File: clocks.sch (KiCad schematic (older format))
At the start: 13 parts, among them J9 UPDI TTL, U10 ATtiny1614-SS, U11 5M1270ZT144C5N, U14 Si5351A-B-GT, X1 CB3LV-3I-100M0000, Y1 25MHZ 8PF

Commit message: parts placement
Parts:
- U10: Description (none) -> 8-bit Microcontrollers - MCU 20MHZ SOIC 85C GRN; MFR (none) -> Microchip Technology; MPN (none) -> ATTINY1614-SSNR; SPN (none) -> 556-ATTINY1614SSNR; SPR (none) -> Mouser; SPURL (none) -> https://www.mouser.com/ProductDetail/556-ATTINY1614SSNR
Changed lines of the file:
@@
 F 2 "Package_SO:SOIC-14_3.9x8.7mm_P1.27mm" H 2150 4660 50  0001 C CIN
 F 3 "http://ww1.microchip.com/downloads/en/DeviceDoc/ATtiny1614-data-sheet-40001995A.pdf" H 2150 4660 50  0001 C CNN
+F 4 "8-bit Microcontrollers - MCU 20MHZ SOIC 85C GRN" H 2150 4660 50  0001 C CNN "Description"
+F 5 "Microchip Technology" H 2150 4660 50  0001 C CNN "MFR"
+F 6 "ATTINY1614-SSNR" H 2150 4660 50  0001 C CNN "MPN"
+F 7 "556-ATTINY1614SSNR" H 2150 4660 50  0001 C CNN "SPN"
+F 8 "Mouser" H 2150 4660 50  0001 C CNN "SPR"
+F 9 "https://www.mouser.com/ProductDetail/556-ATTINY1614SSNR" H 2150 4660 50  0001 C CNN "SPURL"
 	1    2150 4660
 	1    0    0    -1

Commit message: started routing
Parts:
- removed C33: 100nF, Capacitor_SMD:C_0603_1608Metric_Pad1.05x0.95mm_HandSolder, symbol Device:C
- removed R12: 22R5, Resistor_SMD:R_0603_1608Metric_Pad1.05x0.95mm_HandSolder, symbol Device:R_Small
- removed X1: CB3LV-3I-100M0000, Oscillator:Oscillator_SMD_SeikoEpson_SG8002CA-4Pin_7.0x5.0mm_HandSoldering, symbol rc2014_max_v-rescue:CB3LV-3I-50M0000-Oscillator
- J9: footprint Connector_PinHeader_2.54mm:PinHeader_1x03_P2.54mm_Horizontal -> Connector_PinHeader_2.54mm:PinHeader_1x03_P2.54mm_Vertical
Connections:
- net labels added: CLK2_F
- net labels removed: CLK_50Mhz
- wire segments 43 -> 30
- no-connect marks 9 -> 10
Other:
- moved on the sheet: R10, R11, U14, Y1

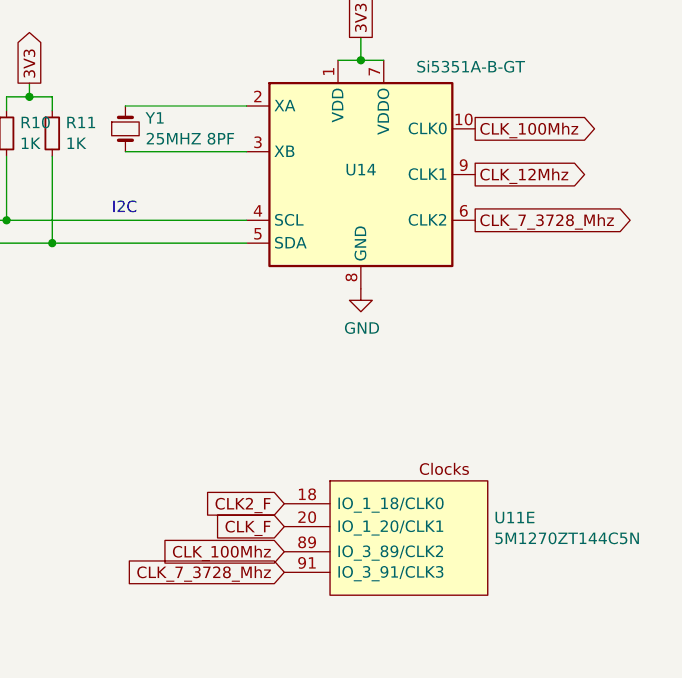
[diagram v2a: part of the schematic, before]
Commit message: moved things around to improve routing, fixed power plane
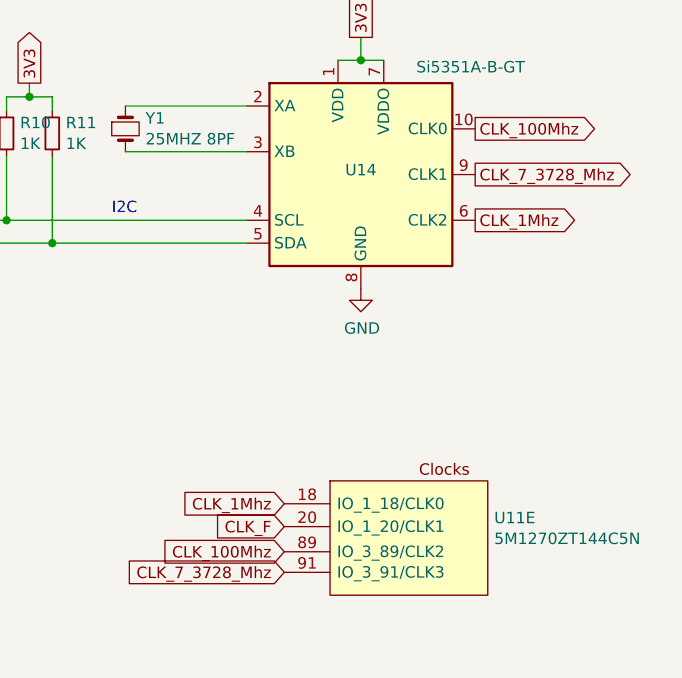
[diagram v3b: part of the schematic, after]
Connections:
- net labels added: CLK_1Mhz
- net labels removed: CLK2_F, CLK_12Mhz
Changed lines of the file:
@@
 CLK_100Mhz
 Text GLabel 6335 1845 2    50   Output ~ 0
-CLK_12Mhz
-Text GLabel 6335 2045 2    50   Output ~ 0
 CLK_7_3728_Mhz
 Text GLabel 4175 2045 0    50   BiDi ~ 0
@@
 NoConn ~ 1550 4460
 NoConn ~ 3415 4055
+Text GLabel 6335 2045 2    50   Output ~ 0
+CLK_1Mhz
 Text GLabel 5500 3285 0    50   Input ~ 0
-CLK2_F
+CLK_1Mhz
 $EndSCHEMATC

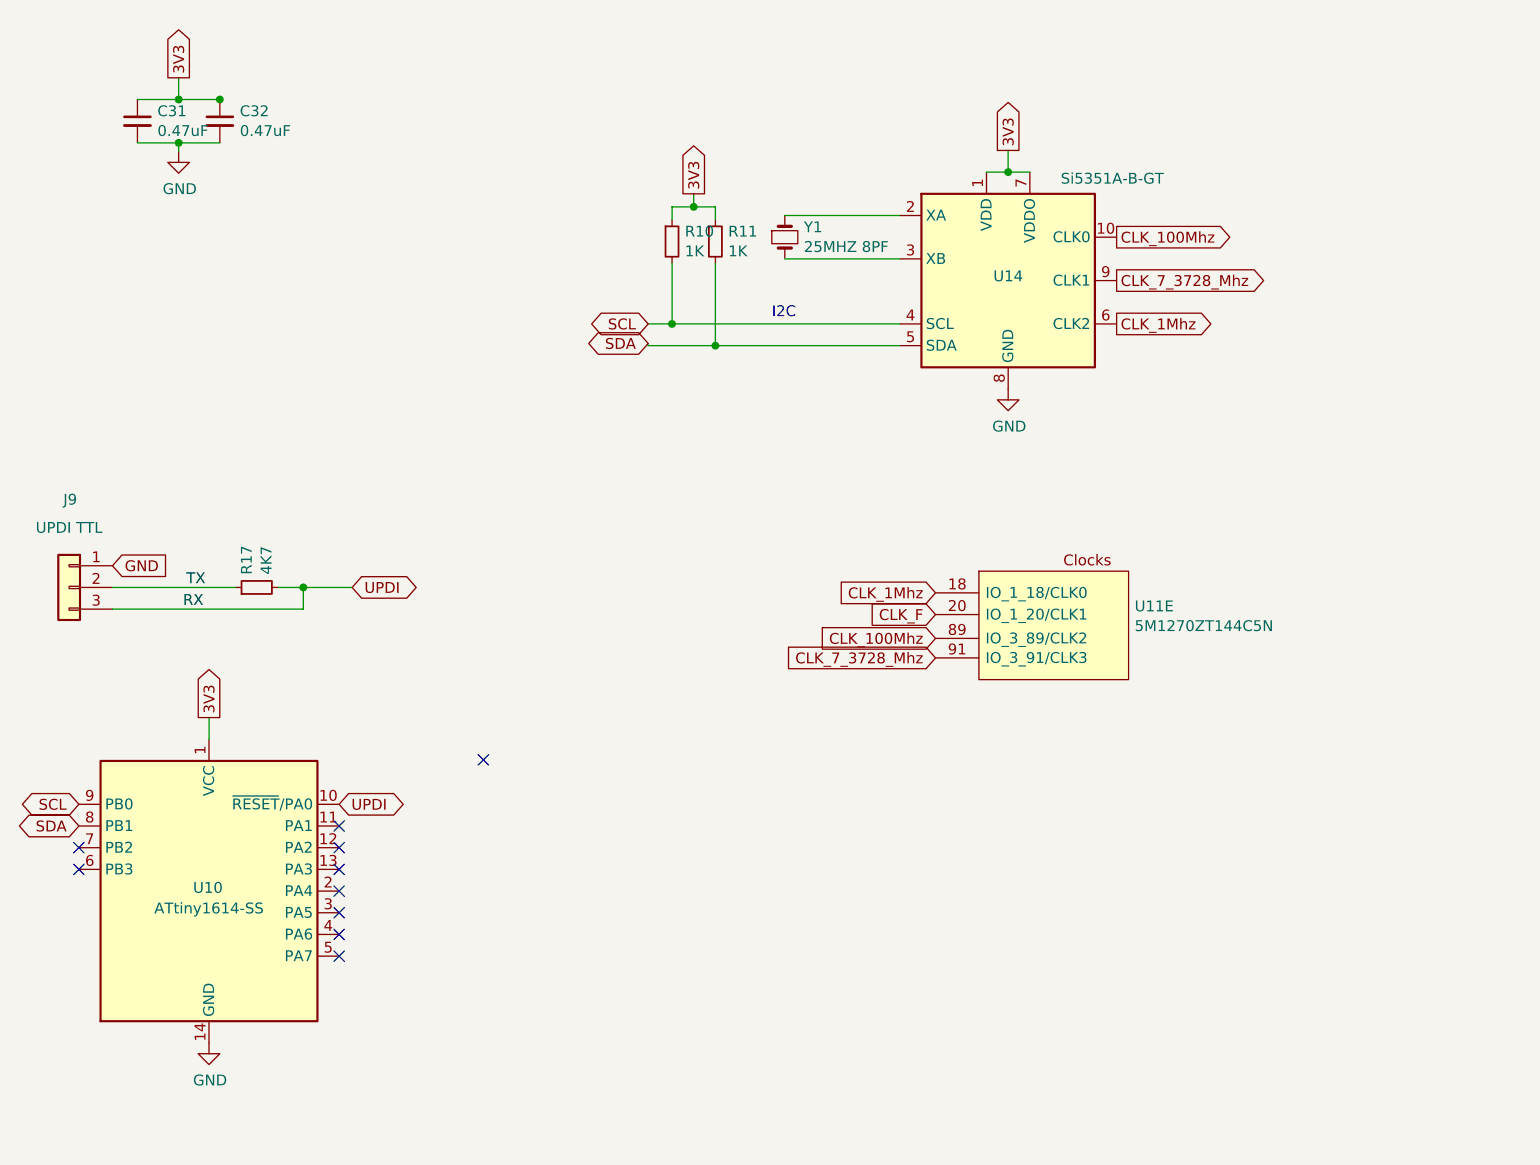
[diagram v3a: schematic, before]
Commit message: replaced some global pins with hierarchical sheet pins
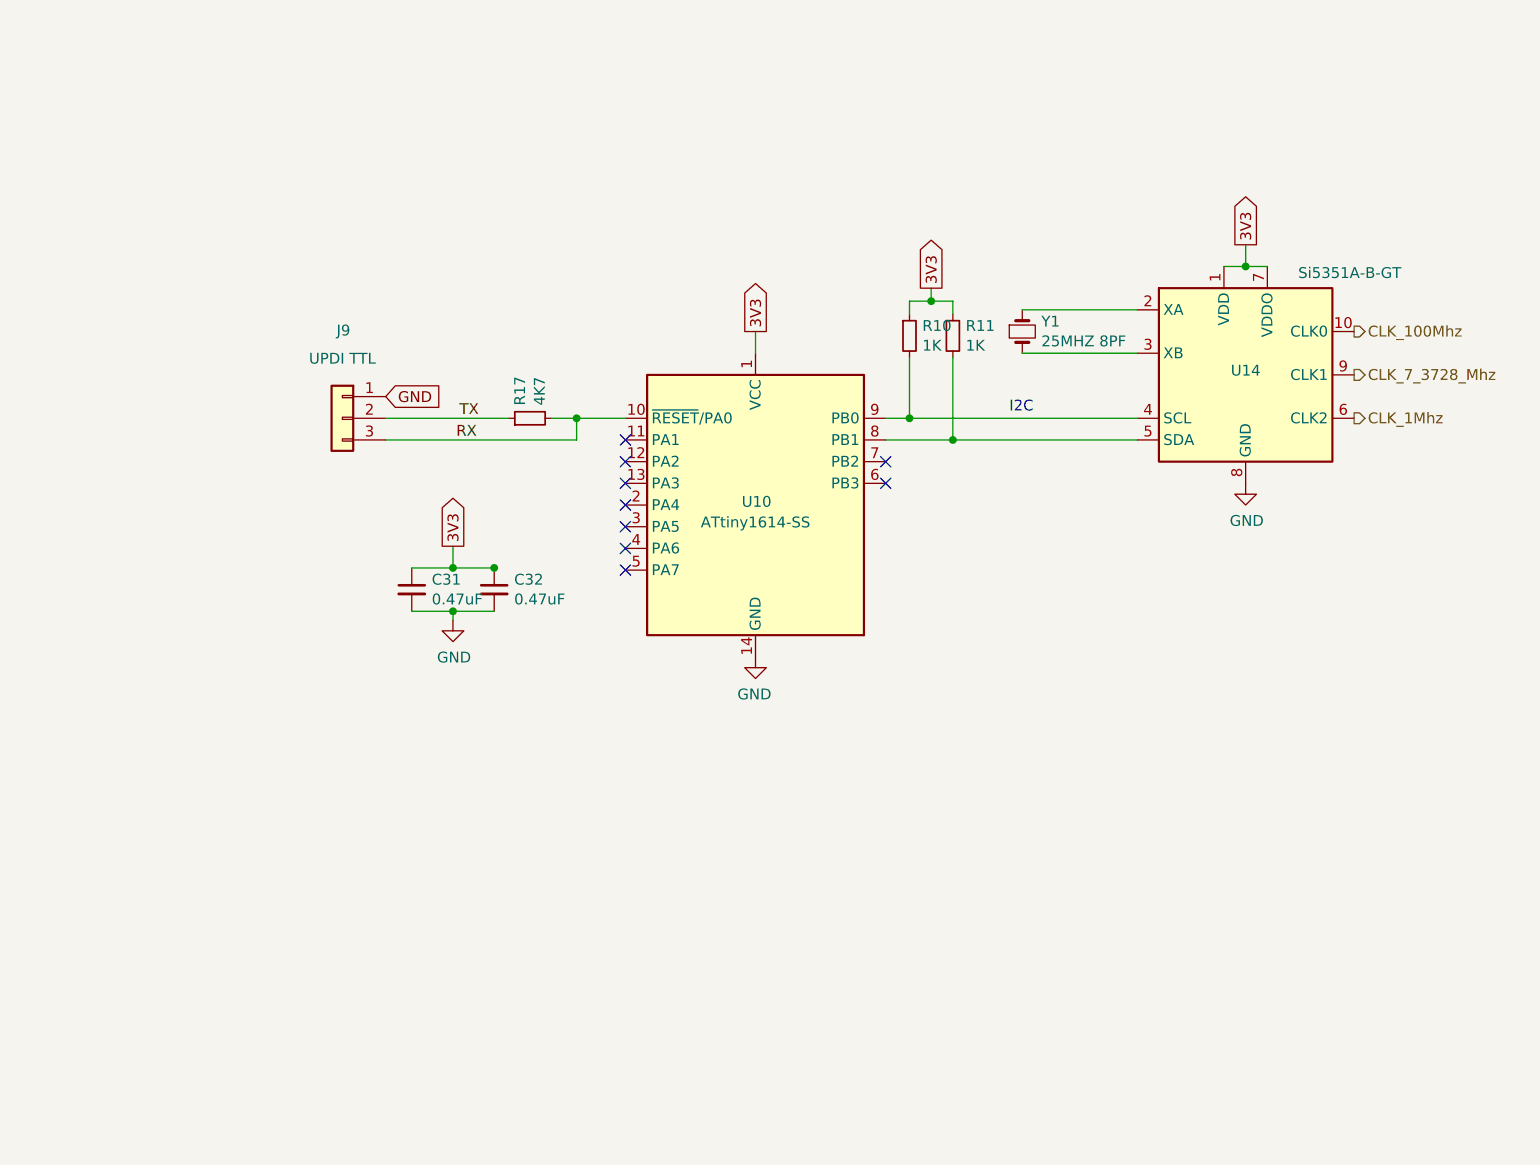
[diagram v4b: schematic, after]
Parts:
- removed U11: 5M1270ZT144C5N, Package_QFP:TQFP-144_20x20mm_P0.5mm, symbol rc2014_max_v-rescue:5M1270ZT144C5N-CPLD_Altera
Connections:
- net labels removed: CLK_F, SCL, SDA, UPDI
- wire segments 30 -> 29
- no-connect marks 10 -> 9
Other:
- moved on the sheet: C31, C32, J9, R10, R11, R17, U10, U14, Y1

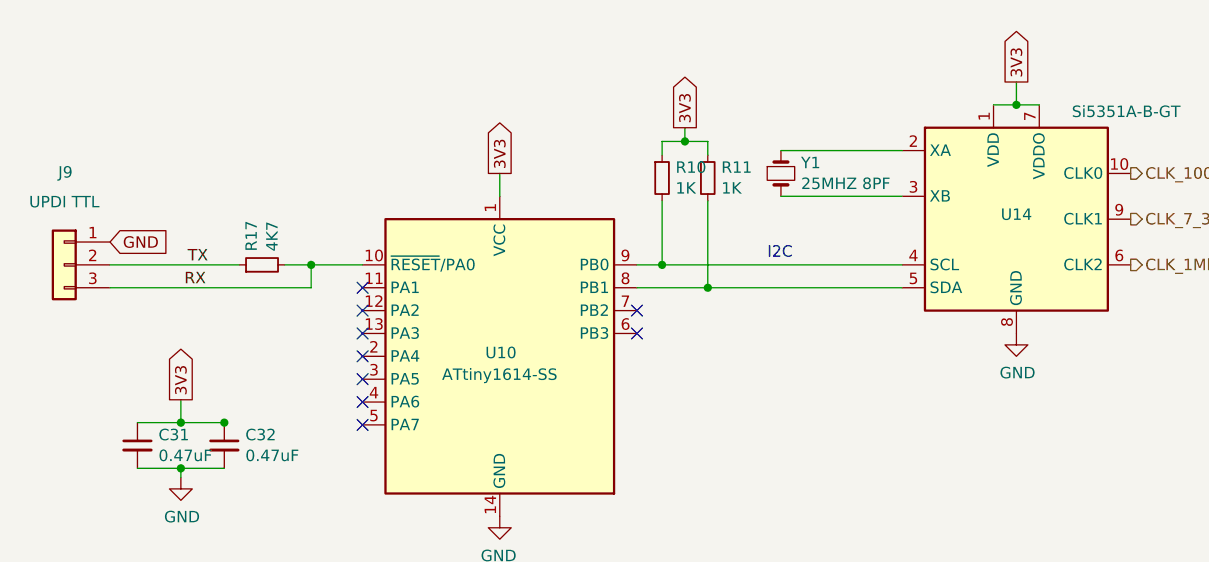
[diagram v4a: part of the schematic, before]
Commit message: Added bus structure, additional pins added, 5V load balancer
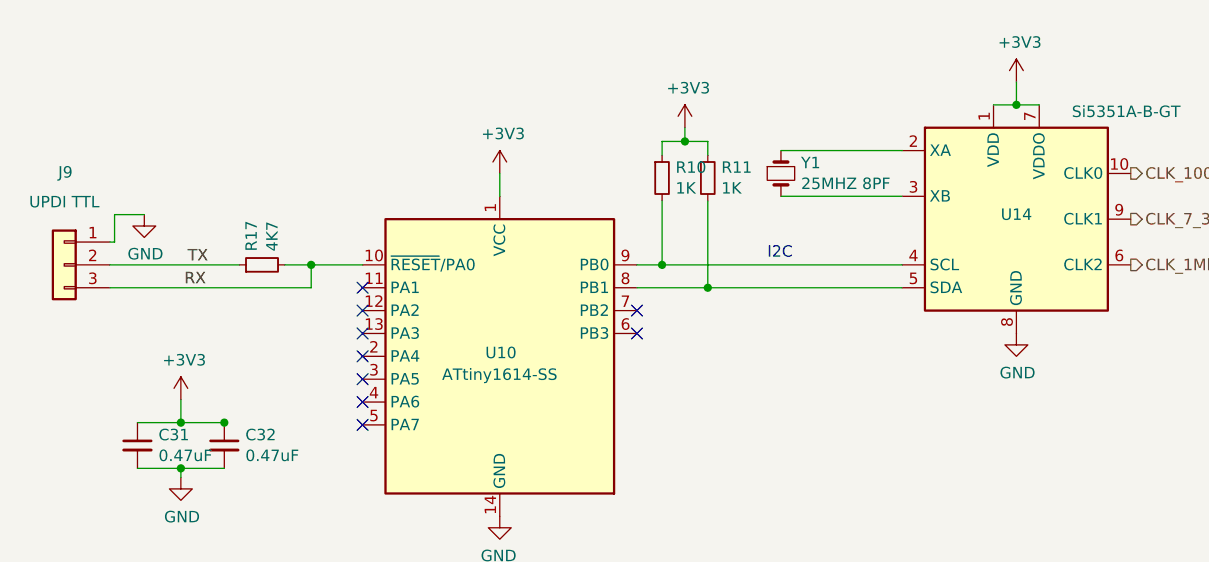
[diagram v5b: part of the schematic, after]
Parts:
- J9: footprint Connector_PinHeader_2.54mm:PinHeader_1x03_P2.54mm_Vertical -> Connector_PinHeader_1.27mm:PinHeader_1x03_P1.27mm_Vertical
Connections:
- net labels added: +3V3
- net labels removed: 3V3
- wire segments 29 -> 32
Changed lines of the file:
@@
 EESchema Schematic File Version 4
 LIBS:rc2014_max_v-cache
+LIBS:sbc_z80-cache
+LIBS:power_share-cache
 EELAYER 29 0
 EELAYER END
@@
 $Comp
 L power:GND #PWR?
-U 1 1 5D00E3D9
+U 1 1 5D255C0F
 P 3275 3410
-AR Path="/5D00E3D9" Ref="#PWR?"  Part="1"
-AR Path="/5D0F9837/5D00E3D9" Ref="#PWR?"  Part="1"
-AR Path="/5CFABACD/5D00E3D9" Ref="#PWR?"  Part="1"
-AR Path="/5CFABACD/5CFFC458/5D00E3D9" Ref="#PWR061"  Part="1"
+AR Path="/5D255C0F" Ref="#PWR?"  Part="1"
+AR Path="/5D0F9837/5D255C0F" Ref="#PWR?"  Part="1"
+AR Path="/5CFABACD/5D255C0F" Ref="#PWR?"  Part="1"
+AR Path="/5CFABACD/5CFFC458/5D255C0F" Ref="#PWR061"  Part="1"
 F 0 "#PWR061" H 3275 3160 50  0001 C CNN
 F 1 "GND" H 3280 3237 50  0000 C CNN
@@
 $Comp
 L Device:R_Small R10
-U 1 1 5D0168D6
+U 1 1 5D255C10
 P 5380 2100
 F 0 "R10" H 5439 2146 50  0000 L CNN
@@
 $Comp
 L Device:R_Small R11
-U 1 1 5D017809
+U 1 1 5D255C11
 P 5580 2100
 F 0 "R11" H 5639 2146 50  0000 L CNN
@@
 Text Notes 5840 2460 0    50   ~ 0
 I2C
-Text GLabel 6930 1680 1    50   Output ~ 0
-3V3
-Text GLabel 3275 3070 1    50   Output ~ 0
-3V3
-Text GLabel 5480 1880 1    50   Output ~ 0
-3V3
 Wire Wire Line
 	6430 1980 5900 1980
@@
 $Comp
 L MCU_Microchip_ATtiny:ATtiny1614-SS U10
-U 1 1 5D018E69
+U 1 1 5D255C12
 P 4670 2880
 F 0 "U10" H 4665 2895 50  0000 C CNN
@@
 	-1   0    0    -1
 $EndComp
-Text GLabel 4670 2080 1    50   Output ~ 0
-3V3
 Wire Wire Line
 	4670 2180 4670 2080
 $Comp
 L power:GND #PWR?
-U 1 1 5D01D4B0
+U 1 1 5D255C13
 P 4670 3580
-AR Path="/5D01D4B0" Ref="#PWR?"  Part="1"
-AR Path="/5D0F9837/5D01D4B0" Ref="#PWR?"  Part="1"
-AR Path="/5CFABACD/5D01D4B0" Ref="#PWR?"  Part="1"
-AR Path="/5CFABACD/5CFFC458/5D01D4B0" Ref="#PWR01"  Part="1"
+AR Path="/5D255C13" Ref="#PWR?"  Part="1"
+AR Path="/5D0F9837/5D255C13" Ref="#PWR?"  Part="1"
+AR Path="/5CFABACD/5D255C13" Ref="#PWR?"  Part="1"
+AR Path="/5CFABACD/5CFFC458/5D255C13" Ref="#PWR01"  Part="1"
 F 0 "#PWR01" H 4670 3330 50  0001 C CNN
 F 1 "GND" H 4675 3407 50  0000 C CNN
@@
 $Comp
 L Connector_Generic:Conn_01x03 J?
-U 1 1 5D03DC78
+U 1 1 5D255C14
 P 2765 2480
-AR Path="/5D03DC78" Ref="J?"  Part="1"
-AR Path="/5CF9C1ED/5D03DC78" Ref="J?"  Part="1"
-AR Path="/5CFABACD/5CFFC458/5D03DC78" Ref="J9"  Part="1"
+AR Path="/5D255C14" Ref="J?"  Part="1"
+AR Path="/5CF9C1ED/5D255C14" Ref="J?"  Part="1"
+AR Path="/5CFABACD/5CFFC458/5D255C14" Ref="J9"  Part="1"
 F 0 "J9" H 2760 2885 50  0000 C CNN
 F 1 "UPDI TTL" H 2765 2755 50  0000 C CNN
-F 2 "Connector_PinHeader_2.54mm:PinHeader_1x03_P2.54mm_Vertical" H 2765 2480 50  0001 C CNN
+F 2 "Connector_PinHeader_1.27mm:PinHeader_1x03_P1.27mm_Vertical" H 2765 2480 50  0001 C CNN
 F 3 "~" H 2765 2480 50  0001 C CNN
 	1    2765 2480
 	-1   0    0    -1
 $EndComp
-Text GLabel 2965 2380 2    50   Input ~ 0
-GND
 Wire Wire Line
 	2965 2480 3530 2480
@@
 $Comp
 L Device:R_Small R17
-U 1 1 5D041A40
+U 1 1 5D255C15
 P 3630 2480
 F 0 "R17" H 3689 2526 50  0000 L CNN
@@
 Text HLabel 7430 2480 2    50   Output ~ 0
 CLK_1Mhz
+$Comp
+L power:+3V3 #PWR?
+U 1 1 5DA0DB4B
+P 4670 2080
+AR Path="/5DA0DB4B" Ref="#PWR?"  Part="1"
+AR Path="/5CFABACD/5CFFC458/5DA0DB4B" Ref="#PWR051"  Part="1"
+F 0 "#PWR051" H 4670 1930 50  0001 C CNN
+F 1 "+3V3" H 4685 2253 50  0000 C CNN
+F 2 "" H 4670 2080 50  0001 C CNN
+F 3 "" H 4670 2080 50  0001 C CNN
+	1    4670 2080
+	1    0    0    -1
+$EndComp
+$Comp
+L power:+3V3 #PWR?
+U 1 1 5DA10138
+P 5480 1880
+AR Path="/5DA10138" Ref="#PWR?"  Part="1"
+AR Path="/5CFABACD/5CFFC458/5DA10138" Ref="#PWR050"  Part="1"
+F 0 "#PWR050" H 5480 1730 50  0001 C CNN
+F 1 "+3V3" H 5495 2053 50  0000 C CNN
+F 2 "" H 5480 1880 50  0001 C CNN
+F 3 "" H 5480 1880 50  0001 C CNN
+	1    5480 1880
+	1    0    0    -1
+$EndComp
+$Comp
+L power:+3V3 #PWR?
+U 1 1 5DA11419
+P 6930 1680
+AR Path="/5DA11419" Ref="#PWR?"  Part="1"
+AR Path="/5CFABACD/5CFFC458/5DA11419" Ref="#PWR049"  Part="1"
+F 0 "#PWR049" H 6930 1530 50  0001 C CNN
+F 1 "+3V3" H 6945 1853 50  0000 C CNN
+F 2 "" H 6930 1680 50  0001 C CNN
+F 3 "" H 6930 1680 50  0001 C CNN
+	1    6930 1680
+	1    0    0    -1
+$EndComp
+$Comp
+L power:+3V3 #PWR?
+U 1 1 5DA128F4
+P 3275 3070
+AR Path="/5DA128F4" Ref="#PWR?"  Part="1"
+AR Path="/5CFABACD/5CFFC458/5DA128F4" Ref="#PWR053"  Part="1"
+F 0 "#PWR053" H 3275 2920 50  0001 C CNN
+F 1 "+3V3" H 3290 3243 50  0000 C CNN
+F 2 "" H 3275 3070 50  0001 C CNN
+F 3 "" H 3275 3070 50  0001 C CNN
+	1    3275 3070
+	1    0    0    -1
+$EndComp
+$Comp
+L power:GND #PWR?
+U 1 1 5DA13F32
+P 3115 2260
+AR Path="/5DA13F32" Ref="#PWR?"  Part="1"
+AR Path="/5D0F9837/5DA13F32" Ref="#PWR?"  Part="1"
+AR Path="/5CFABACD/5DA13F32" Ref="#PWR?"  Part="1"
+AR Path="/5CFABACD/5CFFC458/5DA13F32" Ref="#PWR052"  Part="1"
+F 0 "#PWR052" H 3115 2010 50  0001 C CNN
+F 1 "GND" H 3120 2087 50  0000 C CNN
+F 2 "" H 3115 2260 50  0001 C CNN
+F 3 "" H 3115 2260 50  0001 C CNN
+	1    3115 2260
+	1    0    0    -1
+$EndComp
+Wire Wire Line
+	2965 2380 2985 2380
+Wire Wire Line
+	2985 2380 2985 2260
+Wire Wire Line
+	2985 2260 3115 2260
 $EndSCHEMATC
